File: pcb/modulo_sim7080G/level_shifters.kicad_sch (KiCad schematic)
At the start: 6 parts, among them J2 Conn_01x07, U3 TXB0108PWR

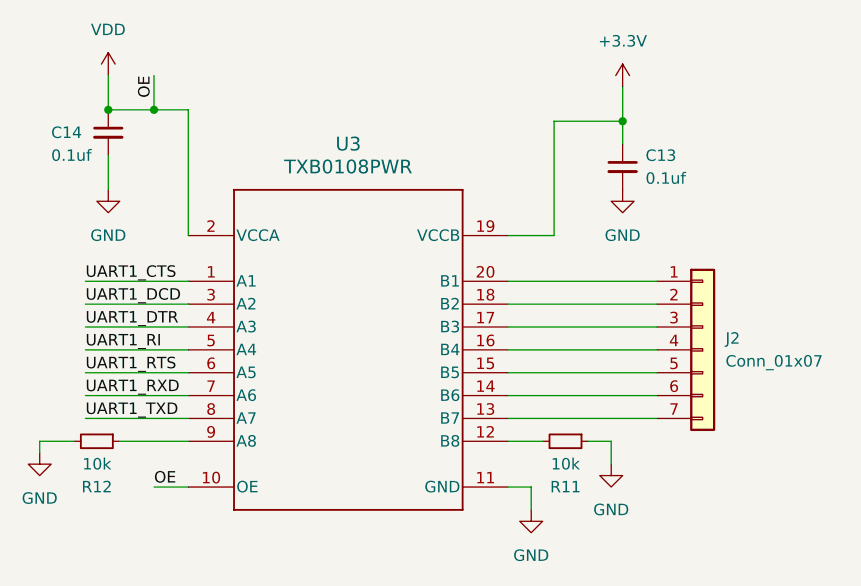
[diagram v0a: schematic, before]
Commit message: se ordenaron los componentes en el pcb
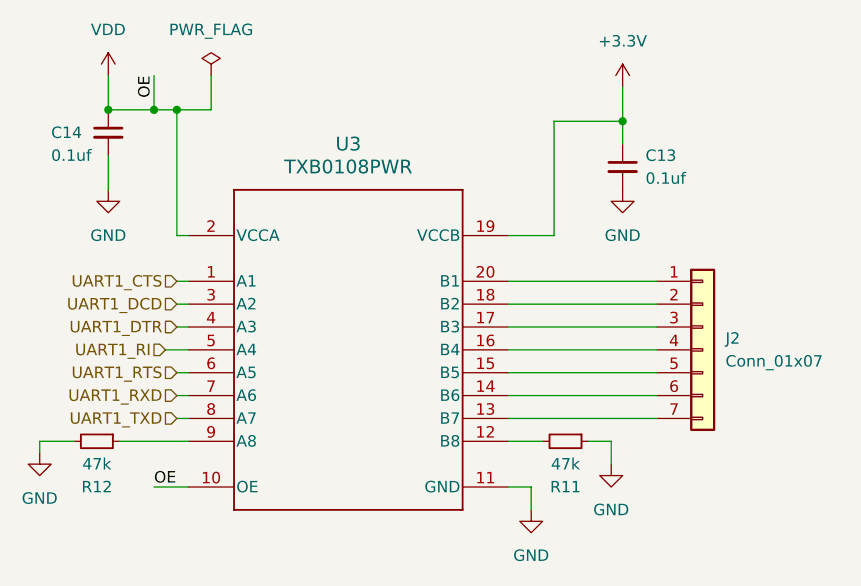
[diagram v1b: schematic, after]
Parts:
- R11, R12: value 10k -> 47k
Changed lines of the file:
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@@
   (junction (at 119.38 57.15) (diameter 0) (color 0 0 0 0)
   )
+  (junction (at 121.92 57.15) (diameter 0) (color 0 0 0 0)
+  )
   (junction (at 171.45 58.42) (diameter 0) (color 0 0 0 0)
   )
@@
     (stroke (width 0) (type default))
   )
-  (wire (pts (xy 111.76 88.9) (xy 123.19 88.9))
-    (stroke (width 0) (type default))
-  )
-  (wire (pts (xy 111.76 83.82) (xy 123.19 83.82))
-    (stroke (width 0) (type default))
-  )
-  (wire (pts (xy 111.76 86.36) (xy 123.19 86.36))
-    (stroke (width 0) (type default))
-  )
-  (wire (pts (xy 111.76 76.2) (xy 123.19 76.2))
+  (wire (pts (xy 120.65 83.82) (xy 123.19 83.82))
+    (stroke (width 0) (type default))
+  )
+  (wire (pts (xy 121.92 86.36) (xy 123.19 86.36))
+    (stroke (width 0) (type default))
+  )
+  (wire (pts (xy 121.92 81.28) (xy 123.19 81.28))
     (stroke (width 0) (type default))
   )
@@
     (stroke (width 0) (type default))
   )
-  (wire (pts (xy 111.76 91.44) (xy 123.19 91.44))
-    (stroke (width 0) (type default))
-  )
   (wire (pts (xy 158.75 99.06) (xy 161.29 99.06))
     (stroke (width 0) (type default))
   )
-  (wire (pts (xy 111.76 78.74) (xy 123.19 78.74))
-    (stroke (width 0) (type default))
-  )
   (wire (pts (xy 171.45 54.61) (xy 171.45 58.42))
     (stroke (width 0) (type default))
   )
+  (wire (pts (xy 121.92 76.2) (xy 123.19 76.2))
+    (stroke (width 0) (type default))
+  )
+  (wire (pts (xy 121.92 91.44) (xy 123.19 91.44))
+    (stroke (width 0) (type default))
+  )
   (wire (pts (xy 110.49 93.98) (xy 106.68 93.98))
     (stroke (width 0) (type default))
@@
     (stroke (width 0) (type default))
   )
+  (wire (pts (xy 125.73 53.34) (xy 125.73 57.15))
+    (stroke (width 0) (type default))
+  )
   (wire (pts (xy 161.29 99.06) (xy 161.29 101.6))
     (stroke (width 0) (type default))
   )
-  (wire (pts (xy 119.38 57.15) (xy 123.19 57.15))
-    (stroke (width 0) (type default))
-  )
-  (wire (pts (xy 111.76 81.28) (xy 123.19 81.28))
+  (wire (pts (xy 119.38 57.15) (xy 121.92 57.15))
     (stroke (width 0) (type default))
   )
@@
     (stroke (width 0) (type default))
   )
-  (wire (pts (xy 123.19 57.15) (xy 123.19 71.12))
+  (wire (pts (xy 121.92 57.15) (xy 121.92 71.12))
     (stroke (width 0) (type default))
   )
@@
     (stroke (width 0) (type default))
   )
+  (wire (pts (xy 121.92 71.12) (xy 123.19 71.12))
+    (stroke (width 0) (type default))
+  )
+  (wire (pts (xy 121.92 88.9) (xy 123.19 88.9))
+    (stroke (width 0) (type default))
+  )
   (wire (pts (xy 158.75 83.82) (xy 175.26 83.82))
     (stroke (width 0) (type default))
@@
     (stroke (width 0) (type default))
   )
-  (label "UART1_RI" (at 111.76 83.82 0) (fields_autoplaced)
-    (effects (font (size 1.27 1.27)) (justify left bottom))
-  )
-  (label "UART1_RTS" (at 111.76 86.36 0) (fields_autoplaced)
-    (effects (font (size 1.27 1.27)) (justify left bottom))
-  )
-  (label "UART1_CTS" (at 111.76 76.2 0) (fields_autoplaced)
-    (effects (font (size 1.27 1.27)) (justify left bottom))
+  (wire (pts (xy 125.73 57.15) (xy 121.92 57.15))
+    (stroke (width 0) (type default))
+  )
+  (wire (pts (xy 121.92 78.74) (xy 123.19 78.74))
+    (stroke (width 0) (type default))
   )
   (label "OE" (at 119.38 53.34 270) (fields_autoplaced)
@@
     (effects (font (size 1.27 1.27)) (justify left bottom))
   )
-  (label "UART1_DCD" (at 111.76 78.74 0) (fields_autoplaced)
-    (effects (font (size 1.27 1.27)) (justify left bottom))
-  )
-  (label "UART1_TXD" (at 111.76 91.44 0) (fields_autoplaced)
-    (effects (font (size 1.27 1.27)) (justify left bottom))
-  )
-  (label "UART1_DTR" (at 111.76 81.28 0) (fields_autoplaced)
-    (effects (font (size 1.27 1.27)) (justify left bottom))
-  )
-  (label "UART1_RXD" (at 111.76 88.9 0) (fields_autoplaced)
-    (effects (font (size 1.27 1.27)) (justify left bottom))
+  (hierarchical_label "UART1_DCD" (shape input) (at 121.92 78.74 180) (fields_autoplaced)
+    (effects (font (size 1.27 1.27)) (justify right))
+  )
+  (hierarchical_label "UART1_RI" (shape input) (at 120.65 83.82 180) (fields_autoplaced)
+    (effects (font (size 1.27 1.27)) (justify right))
+  )
+  (hierarchical_label "UART1_CTS" (shape input) (at 121.92 76.2 180) (fields_autoplaced)
+    (effects (font (size 1.27 1.27)) (justify right))
+  )
+  (hierarchical_label "UART1_TXD" (shape input) (at 121.92 91.44 180) (fields_autoplaced)
+    (effects (font (size 1.27 1.27)) (justify right))
+  )
+  (hierarchical_label "UART1_RTS" (shape input) (at 121.92 86.36 180) (fields_autoplaced)
+    (effects (font (size 1.27 1.27)) (justify right))
+  )
+  (hierarchical_label "UART1_RXD" (shape input) (at 121.92 88.9 180) (fields_autoplaced)
+    (effects (font (size 1.27 1.27)) (justify right))
+  )
+  (hierarchical_label "UART1_DTR" (shape input) (at 121.92 81.28 180) (fields_autoplaced)
+    (effects (font (size 1.27 1.27)) (justify right))
   )
   (symbol (lib_id "Device:C_Small") (at 114.3 59.69 0) (unit 1)
@@
       (effects (font (size 1.27 1.27)))
     )
-    (property "Value" "10k" (at 165.1 96.52 90)
+    (property "Value" "47k" (at 165.1 96.52 90)
       (effects (font (size 1.27 1.27)))
     )
@@
         (path "/1dcf7a25-8a74-4740-bf1e-5ce6cda88171/a3b3018c-0f3b-4301-9cd1-247f073552ff"
           (reference "R11") (unit 1)
+        )
+      )
+    )
+  )
+  (symbol (lib_id "power:PWR_FLAG") (at 125.73 53.34 0) (unit 1)
+    (in_bom yes) (on_board yes) (dnp no) (fields_autoplaced)
+    (property "Reference" "#FLG02" (at 125.73 51.435 0)
+      (effects (font (size 1.27 1.27)) hide)
+    )
+    (property "Value" "PWR_FLAG" (at 125.73 48.26 0)
+      (effects (font (size 1.27 1.27)))
+    )
+    (property "Footprint" "" (at 125.73 53.34 0)
+      (effects (font (size 1.27 1.27)) hide)
+    )
+    (property "Datasheet" "~" (at 125.73 53.34 0)
+      (effects (font (size 1.27 1.27)) hide)
+    )
+    (pin "1")
+    (instances
+      (project "modulo_sim7080G"
+        (path "/1dcf7a25-8a74-4740-bf1e-5ce6cda88171/a3b3018c-0f3b-4301-9cd1-247f073552ff"
+          (reference "#FLG02") (unit 1)
         )
       )
@@
       (effects (font (size 1.27 1.27)))
     )
-    (property "Value" "10k" (at 113.03 96.52 90)
-      (effects (font (size 1.27 1.27)))
-    )
+    (property "Value" "47k" (at 113.03 96.52 90)
+      (effects (font (size 1.27 1.27)))
+    )
